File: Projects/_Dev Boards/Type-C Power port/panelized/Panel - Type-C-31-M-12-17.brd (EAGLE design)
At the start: 100 x 100 mm, 12 parts, among them J1 USB-TYPE-C-31-M-17, J2 USB-TYPE-C-31-M-17, J3 USB-TYPE-C-31-M-17

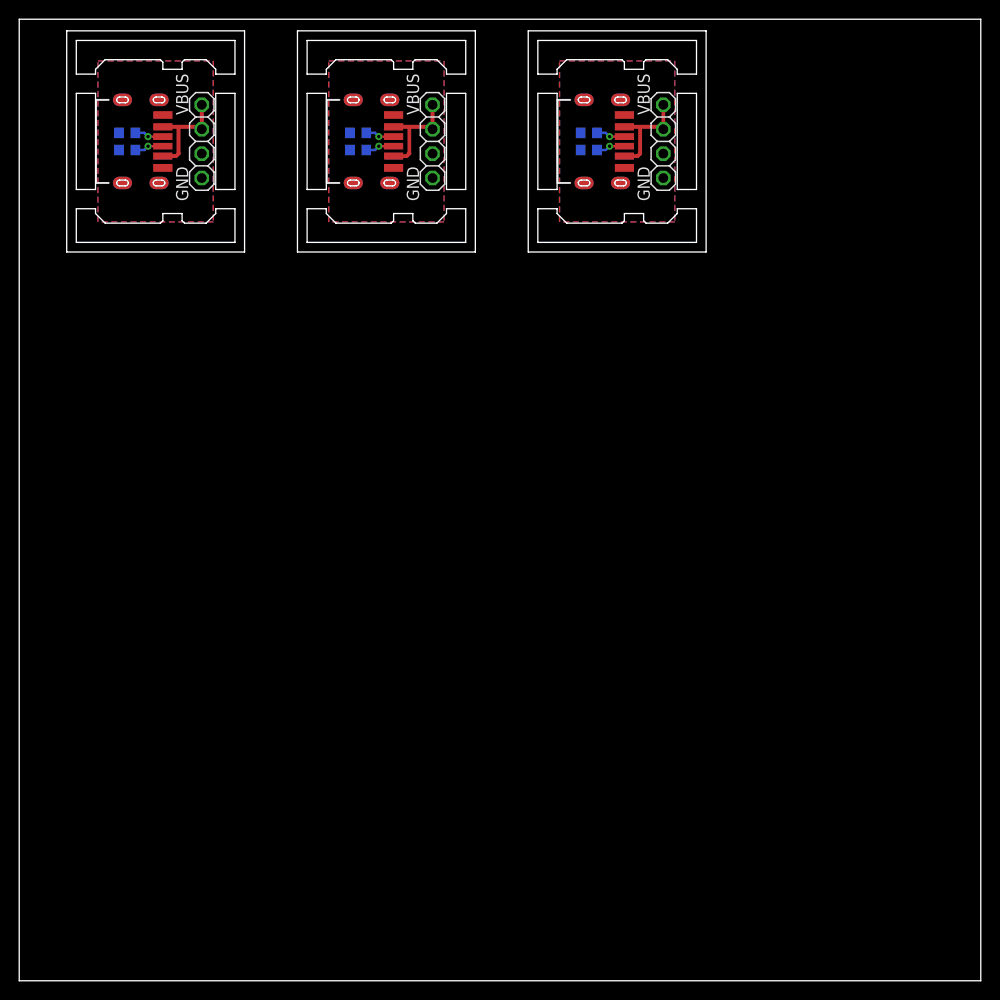
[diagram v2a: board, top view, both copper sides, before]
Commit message: Type-C power port
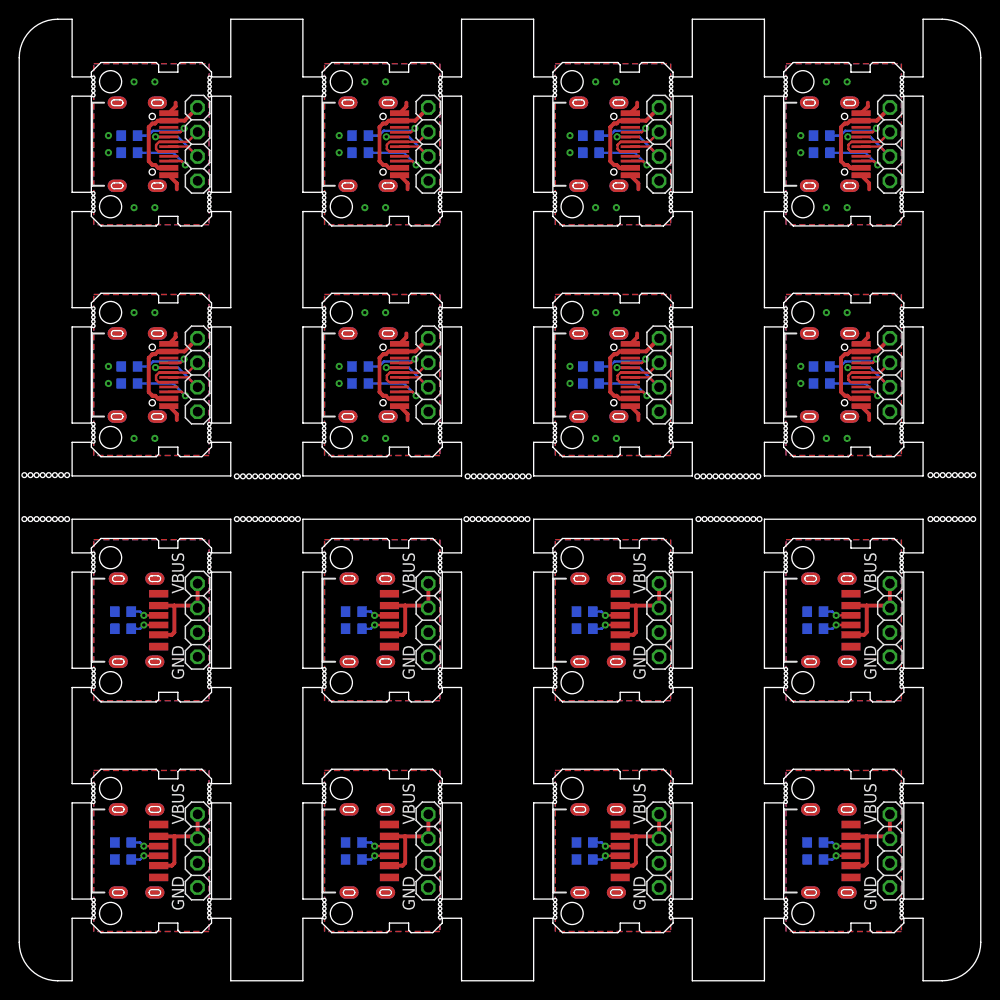
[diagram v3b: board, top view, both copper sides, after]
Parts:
- added J10, J11, J12, J13, J14, J15, J16, J9: USB-TYPE-C-31-M-17, angrypig7-Connectors:USB-TYPE-C-31-M-17
- added J4, J5, J6, J7, J8: USB-TYPE-C-31-M-12, angrypig7-Connectors:USB-TYPE-C-31-M-12
- added JP10, JP11, JP12, JP13, JP14, JP15, JP16, JP4, JP5, JP6, JP7, JP8, JP9: (no value), angrypig7-Connectors-PinHeads:1X04
- added R10, R11, R12, R13, R14, R15, R16, R17, R18, R19, R20, R21, R22, R23, R24, R25, R26, R27, R28, R29, R30, R31, R32, R7, R8, R9: 5.1k, angrypig7-RCL:R0603
- J1, J2, J3: value USB-TYPE-C-31-M-17 -> USB-TYPE-C-31-M-12; device angrypig7-Connectors:USB-TYPE-C-31-M-17 -> angrypig7-Connectors:USB-TYPE-C-31-M-12
- moved JP1 0.52 mm to (18.5, 87.0)
- moved JP2 0.52 mm to (42.5, 87.0)
- moved JP3 0.52 mm to (66.5, 87.0)
- moved R3 0.37 mm to (35.5, 87.9)
- moved R4 0.37 mm to (35.5, 86.1)
- moved R5 0.37 mm to (59.5, 87.9)
- moved R6 0.37 mm to (59.5, 86.1)
- moved R1 0.37 mm to (11.5, 87.9)
- moved R2 0.37 mm to (11.5, 86.1)
- moved J1 0.34 mm to (14.4, 87.0)
- moved J2 0.34 mm to (38.4, 87.0)
- moved J3 0.34 mm to (62.4, 87.0)
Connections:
- new net GND10: J11.GND, J11.GND_2, J11.SHLD-B1, J11.SHLD-B2, J11.SHLD-B3, J11.SHLD-B4, J11.SHLD-T1, J11.SHLD-T2, J11.SHLD-T3, J11.SHLD-T4, JP11.3, JP11.4, R21.2, R22.2
- new net GND11: J12.GND, J12.GND_2, J12.SHLD-B1, J12.SHLD-B2, J12.SHLD-B3, J12.SHLD-B4, J12.SHLD-T1, J12.SHLD-T2, J12.SHLD-T3, J12.SHLD-T4, JP12.3, JP12.4, R23.2, R24.2
- new net GND12: J13.GND, J13.GND_2, J13.SHLD-B1, J13.SHLD-B2, J13.SHLD-B3, J13.SHLD-B4, J13.SHLD-T1, J13.SHLD-T2, J13.SHLD-T3, J13.SHLD-T4, JP13.3, JP13.4, R25.2, R26.2
- new net GND13: J14.GND, J14.GND_2, J14.SHLD-B1, J14.SHLD-B2, J14.SHLD-B3, J14.SHLD-B4, J14.SHLD-T1, J14.SHLD-T2, J14.SHLD-T3, J14.SHLD-T4, JP14.3, JP14.4, R27.2, R28.2
- new net GND14: J15.GND, J15.GND_2, J15.SHLD-B1, J15.SHLD-B2, J15.SHLD-B3, J15.SHLD-B4, J15.SHLD-T1, J15.SHLD-T2, J15.SHLD-T3, J15.SHLD-T4, JP15.3, JP15.4, R29.2, R30.2
- new net GND15: J16.GND, J16.GND_2, J16.SHLD-B1, J16.SHLD-B2, J16.SHLD-B3, J16.SHLD-B4, J16.SHLD-T1, J16.SHLD-T2, J16.SHLD-T3, J16.SHLD-T4, JP16.3, JP16.4, R31.2, R32.2
- new net GND3: J4.GND1, J4.GND2, J4.SHLD-B1, J4.SHLD-B2, J4.SHLD-B3, J4.SHLD-B4, J4.SHLD-T1, J4.SHLD-T2, J4.SHLD-T3, J4.SHLD-T4, JP4.4, R7.2, R8.2
- new net GND4: J5.GND1, J5.GND2, J5.SHLD-B1, J5.SHLD-B2, J5.SHLD-B3, J5.SHLD-B4, J5.SHLD-T1, J5.SHLD-T2, J5.SHLD-T3, J5.SHLD-T4, JP5.4, R10.2, R9.2
- new net GND5: J6.GND1, J6.GND2, J6.SHLD-B1, J6.SHLD-B2, J6.SHLD-B3, J6.SHLD-B4, J6.SHLD-T1, J6.SHLD-T2, J6.SHLD-T3, J6.SHLD-T4, JP6.4, R11.2, R12.2
- new net GND6: J7.GND1, J7.GND2, J7.SHLD-B1, J7.SHLD-B2, J7.SHLD-B3, J7.SHLD-B4, J7.SHLD-T1, J7.SHLD-T2, J7.SHLD-T3, J7.SHLD-T4, JP7.4, R13.2, R14.2
- new net GND7: J8.GND1, J8.GND2, J8.SHLD-B1, J8.SHLD-B2, J8.SHLD-B3, J8.SHLD-B4, J8.SHLD-T1, J8.SHLD-T2, J8.SHLD-T3, J8.SHLD-T4, JP8.4, R15.2, R16.2
- new net GND8: J9.GND, J9.GND_2, J9.SHLD-B1, J9.SHLD-B2, J9.SHLD-B3, J9.SHLD-B4, J9.SHLD-T1, J9.SHLD-T2, J9.SHLD-T3, J9.SHLD-T4, JP9.3, JP9.4, R17.2, R18.2
- new net GND9: J10.GND, J10.GND_2, J10.SHLD-B1, J10.SHLD-B2, J10.SHLD-B3, J10.SHLD-B4, J10.SHLD-T1, J10.SHLD-T2, J10.SHLD-T3, J10.SHLD-T4, JP10.3, JP10.4, R19.2, R20.2
- new net N$10: J3.A7, J3.B7, JP3.3
- new net N$11: J3.A5, R5.1
- new net N$12: J3.B5, R6.1
- new net N$13: J4.A6, J4.B6, JP4.2
- new net N$14: J4.A7, J4.B7, JP4.3
- new net N$15: J4.A5, R7.1
- new net N$16: J4.B5, R8.1
- new net N$17: J5.A6, J5.B6, JP5.2
- new net N$18: J5.A7, J5.B7, JP5.3
- new net N$19: J5.A5, R9.1
- new net N$20: J5.B5, R10.1
- new net N$21: J6.A6, J6.B6, JP6.2
- new net N$22: J6.A7, J6.B7, JP6.3
- new net N$23: J6.A5, R11.1
- new net N$24: J6.B5, R12.1
- new net N$25: J7.A6, J7.B6, JP7.2
- new net N$26: J7.A7, J7.B7, JP7.3
- new net N$27: J7.A5, R13.1
- new net N$28: J7.B5, R14.1
- new net N$29: J8.A6, J8.B6, JP8.2
- new net N$30: J8.A7, J8.B7, JP8.3
- new net N$31: J8.A5, R15.1
- new net N$32: J8.B5, R16.1
- new net N$33: J9.CC1, R17.1
- new net N$34: J9.CC2, R18.1
- new net N$35: J10.CC1, R19.1
- new net N$36: J10.CC2, R20.1
- new net N$37: J11.CC1, R21.1
- new net N$38: J11.CC2, R22.1
- new net N$39: J12.CC1, R23.1
- new net N$40: J12.CC2, R24.1
- new net N$41: J13.CC1, R25.1
- new net N$42: J13.CC2, R26.1
- new net N$43: J14.CC1, R27.1
- new net N$44: J14.CC2, R28.1
- new net N$45: J15.CC1, R29.1
- new net N$46: J15.CC2, R30.1
- new net N$47: J16.CC1, R31.1
- new net N$48: J16.CC2, R32.1
- new net N$7: J2.A5, R3.1
- new net N$8: J2.B5, R4.1
- new net N$9: J3.A6, J3.B6, JP3.2
- new net VBUS10: J11.VBUS, J11.VBUS_2, JP11.1, JP11.2
- new net VBUS11: J12.VBUS, J12.VBUS_2, JP12.1, JP12.2
- new net VBUS12: J13.VBUS, J13.VBUS_2, JP13.1, JP13.2
- new net VBUS13: J14.VBUS, J14.VBUS_2, JP14.1, JP14.2
- new net VBUS14: J15.VBUS, J15.VBUS_2, JP15.1, JP15.2
- new net VBUS15: J16.VBUS, J16.VBUS_2, JP16.1, JP16.2
- new net VBUS3: J4.VBUS1, J4.VBUS2, JP4.1
- new net VBUS4: J5.VBUS1, J5.VBUS2, JP5.1
- new net VBUS5: J6.VBUS1, J6.VBUS2, JP6.1
- new net VBUS6: J7.VBUS1, J7.VBUS2, JP7.1
- new net VBUS7: J8.VBUS1, J8.VBUS2, JP8.1
- new net VBUS8: J9.VBUS, J9.VBUS_2, JP9.1, JP9.2
- new net VBUS9: J10.VBUS, J10.VBUS_2, JP10.1, JP10.2
- net GND: now also J1.GND1, J1.GND2; no longer J1.GND, J1.GND_2, JP1.3
- net GND1: now also J2.GND1, J2.GND2; no longer J2.GND, J2.GND_2, JP2.3
- net GND2: now also J3.GND1, J3.GND2; no longer J3.GND, J3.GND_2, JP3.3
- net N$1: now also J2.A6, J2.B6, JP2.2; no longer J1.CC1, R1.1
- net N$2: now also J1.A6, J1.B6, JP1.2; no longer J1.CC2, R2.1
- net N$3: now also J1.A7, J1.B7, JP1.3; no longer J2.CC1, R3.1
- net N$4: now also J2.A7, J2.B7, JP2.3; no longer J2.CC2, R4.1
- net N$5: now also J1.A5, R1.1; no longer J3.CC1, R5.1
- net N$6: now also J1.B5, R2.1; no longer J3.CC2, R6.1
- net VBUS: now also J1.VBUS1, J1.VBUS2; no longer J1.VBUS, J1.VBUS_2, JP1.2
- net VBUS1: now also J2.VBUS1, J2.VBUS2; no longer J2.VBUS, J2.VBUS_2, JP2.2
- net VBUS2: now also J3.VBUS1, J3.VBUS2; no longer J3.VBUS, J3.VBUS_2, JP3.2
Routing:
- net VBUS7: track 0.00 -> 11.8 mm
- net VBUS3: track 0.00 -> 11.8 mm
- net VBUS4: track 0.00 -> 11.8 mm
- net VBUS6: track 0.00 -> 11.8 mm
- net VBUS5: track 0.00 -> 11.8 mm
- net VBUS10: track 0.00 -> 11.2 mm
- net VBUS9: track 0.00 -> 11.2 mm
- net VBUS14: track 0.00 -> 11.2 mm
- net VBUS8: track 0.00 -> 11.2 mm
- net VBUS13: track 0.00 -> 11.2 mm
- net VBUS12: track 0.00 -> 11.2 mm
- net VBUS11: track 0.00 -> 11.2 mm
- net VBUS15: track 0.00 -> 11.2 mm
- net N$30: track 0.00 -> 10.0 mm, vias 0 -> 1
- net N$26: track 0.00 -> 10.0 mm, vias 0 -> 1
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- added copper zone on layer 1, net GND10
- added copper zone on layer 16, net GND10
- added copper zone on layer 1, net GND11
- added copper zone on layer 16, net GND11
- added copper zone on layer 1, net GND12
- added copper zone on layer 16, net GND12
- added copper zone on layer 1, net GND13
- added copper zone on layer 16, net GND13
- added copper zone on layer 1, net GND14
- added copper zone on layer 16, net GND14
- added copper zone on layer 1, net GND15
- added copper zone on layer 16, net GND15
- added copper zone on layer 1, net GND3
- added copper zone on layer 16, net GND3
- added copper zone on layer 1, net GND4
- added copper zone on layer 16, net GND4
- added copper zone on layer 1, net GND5
- added copper zone on layer 16, net GND5
- added copper zone on layer 1, net GND6
- added copper zone on layer 16, net GND6
- added copper zone on layer 1, net GND7
- added copper zone on layer 16, net GND7
- added copper zone on layer 1, net GND8
- added copper zone on layer 16, net GND8
- added copper zone on layer 1, net GND9
- added copper zone on layer 16, net GND9
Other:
- outline, holes or cut-outs redrawn
- board text added: "D+"
- board text added: "D-"
